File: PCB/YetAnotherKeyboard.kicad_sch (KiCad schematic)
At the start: 15 parts, among them SW88 SW_SPDT, U1 TP4056-42-ESOP8, U2 ER_OLEDM0.91_1x-I2C

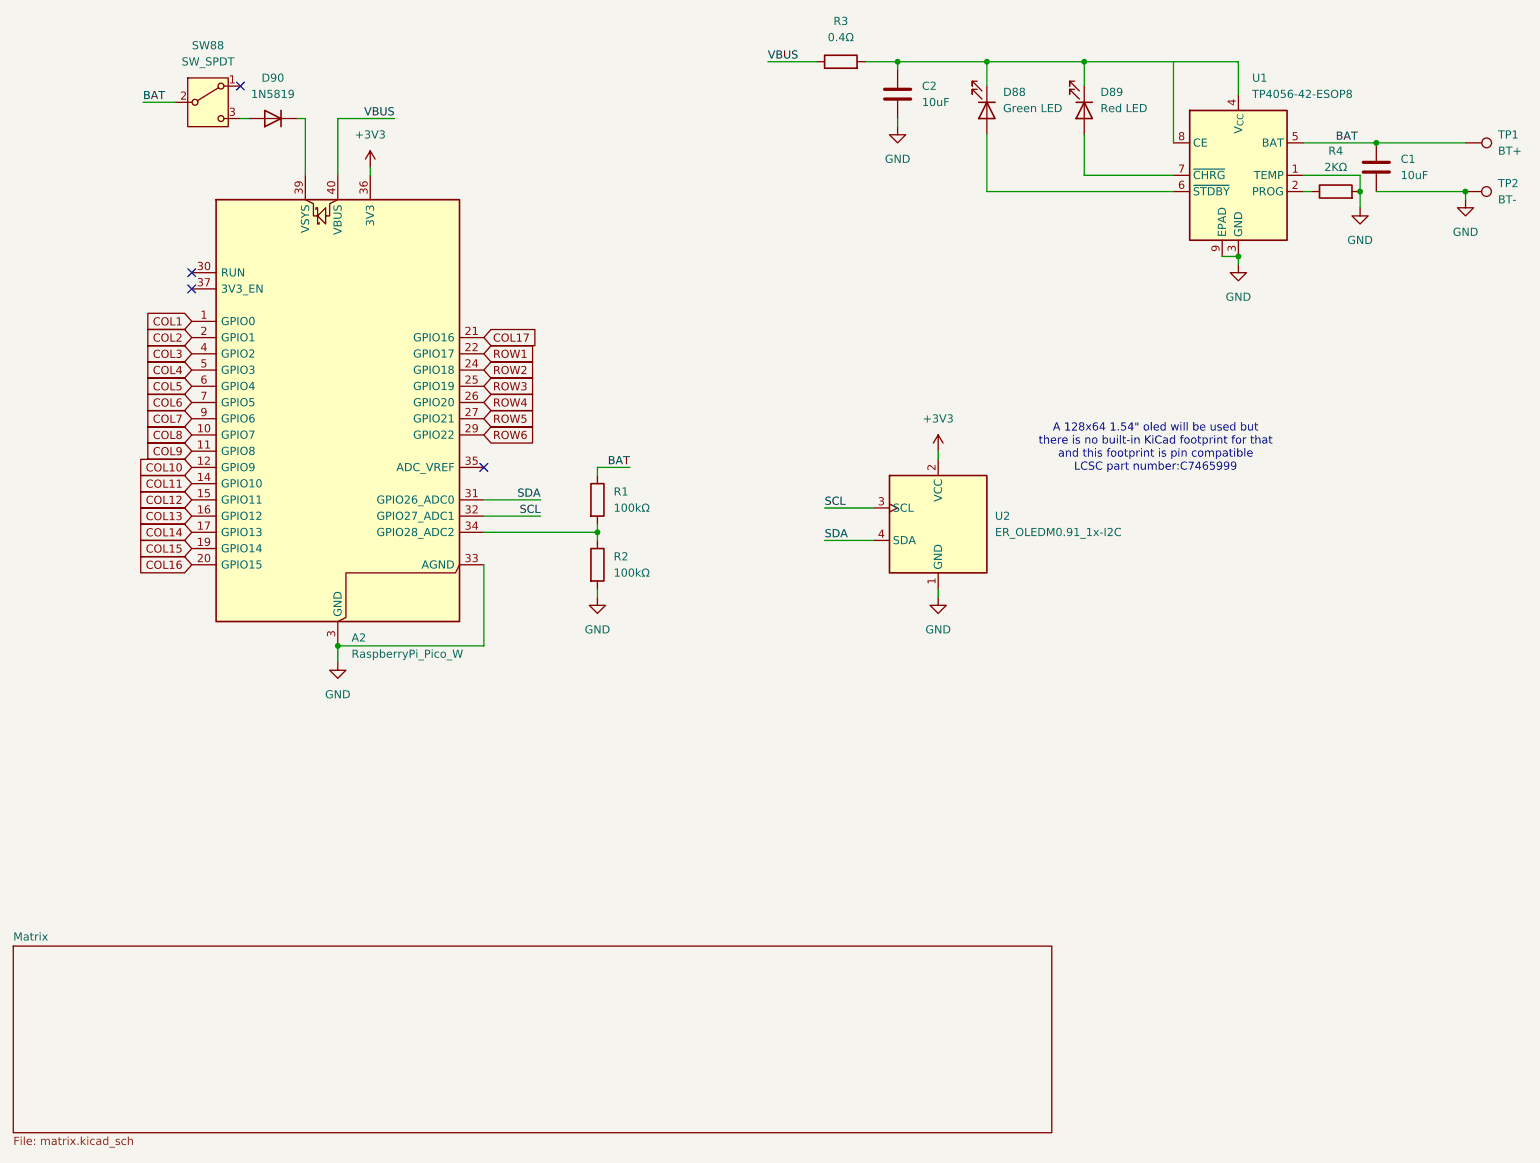
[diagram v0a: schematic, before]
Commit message: change schema to nice! compenents
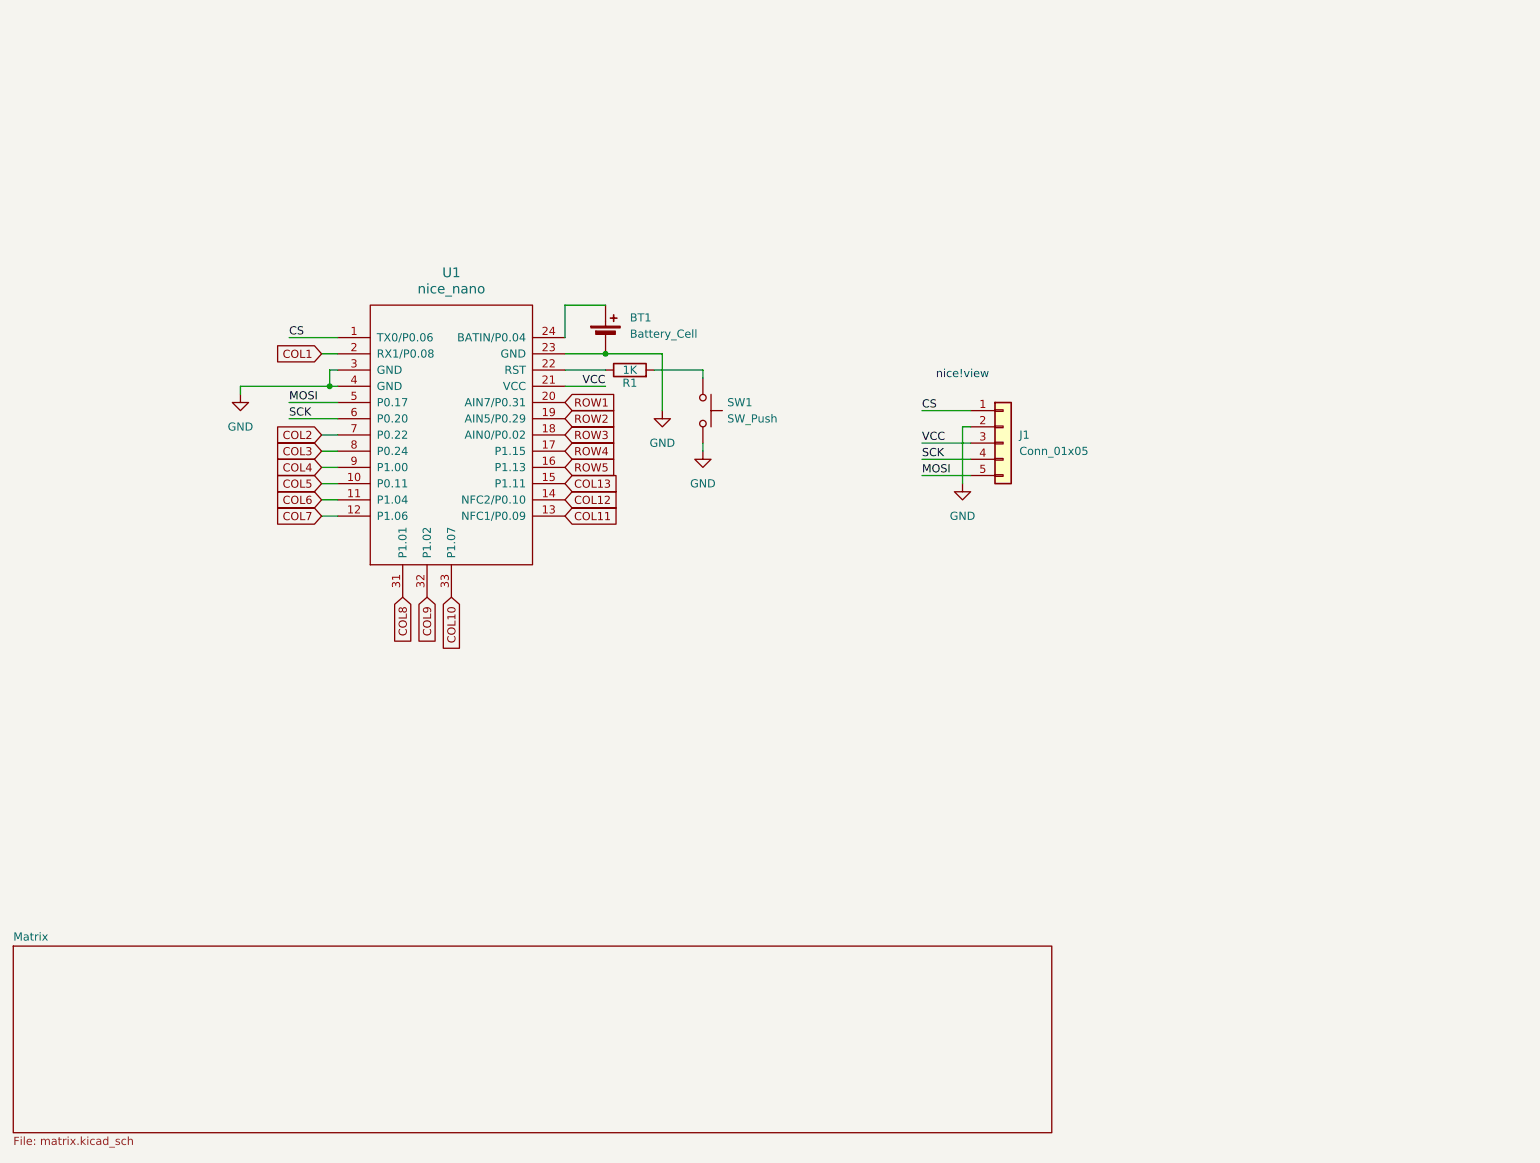
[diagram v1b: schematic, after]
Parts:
- removed A2: RaspberryPi_Pico_W, Module:RaspberryPi_Pico_W_SMD_HandSolder, symbol MCU_Module:RaspberryPi_Pico_W
- removed C1, C2: 10uF, Capacitor_SMD:C_0402_1005Metric, symbol Device:C
- removed D88: Green LED, LED_SMD:LED_0603_1608Metric, symbol Device:LED
- removed D89: Red LED, LED_SMD:LED_0603_1608Metric, symbol Device:LED
- removed D90: 1N5819, Diode_THT:D_DO-41_SOD81_P7.62mm_Horizontal, symbol Device:D
- removed R2: 100kΩ, Resistor_SMD:R_0402_1005Metric, symbol Device:R
- removed R3: 0.4Ω, Resistor_SMD:R_0402_1005Metric, symbol Device:R
- removed R4: 2KΩ, Resistor_SMD:R_0402_1005Metric, symbol Device:R
- removed SW88: SW_SPDT, Button_Switch_SMD:SW_SPDT_Shouhan_MSK12C02, symbol Switch:SW_SPDT
- removed TP1: BT+, TestPoint:TestPoint_Pad_D4.0mm, symbol Connector:TestPoint
- removed TP2: BT-, TestPoint:TestPoint_Pad_D4.0mm, symbol Connector:TestPoint
- removed U1: TP4056-42-ESOP8, Package_SO:SOIC-8-1EP_3.9x4.9mm_P1.27mm_EP2.41x3.3mm_ThermalVias, symbol Battery_Management:TP4056-42-ESOP8
- removed U2: ER_OLEDM0.91_1x-I2C, Display:ER_OLEDM0.91_1x-I2C, symbol Display_Graphic:ER_OLEDM0.91_1x-I2C
- added BT1: Battery_Cell, symbol Device:Battery_Cell
- added J1: Conn_01x05, symbol Connector_Generic:Conn_01x05
- added SW1: SW_Push, symbol Switch:SW_Push
- added U1: nice_nano, symbol nice_nano:nice_nano
- R1: value 100kΩ -> 1K; footprint Resistor_SMD:R_0402_1005Metric -> (none)
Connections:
- net COL1: now also U1.2 (RX1/P0.08)
- net COL10: now also U1.33 (P1.07)
- net COL11: now also U1.13 (NFC1/P0.09)
- net COL12: now also U1.14 (NFC2/P0.10)
- net COL13: now also U1.15 (P1.11)
- net COL2: now also U1.7 (P0.22)
- net COL3: now also U1.8 (P0.24)
- net COL4: now also U1.9 (P1.00)
- net COL5: now also U1.10 (P0.11)
- net COL6: now also U1.11 (P1.04)
- net COL7: now also U1.12 (P1.06)
- net COL8: now also U1.31 (P1.01)
- net COL9: now also U1.32 (P1.02)
- net GND: now also BT1.2 (-), J1.2 (Pin_2), SW1.2, U1.23 (GND), U1.3 (GND), U1.4 (GND)
- net ROW1: now also U1.20 (AIN7/P0.31)
- net ROW2: now also U1.19 (AIN5/P0.29)
- net ROW3: now also U1.18 (AIN0/P0.02)
- net ROW4: now also U1.17 (P1.15)
- net ROW5: now also U1.16 (P1.13)
- net at R1.2: now also SW1.1
- net BAT: no longer names the net of R1.1
- net BAT: now also U1.22 (RST)
- new net: BT1.1 (+), U1.24 (BATIN/P0.04)
- new net CS: J1.1 (Pin_1), U1.1 (TX0/P0.06)
- new net MOSI: J1.5 (Pin_5), U1.5 (P0.17)
- new net SCK: J1.4 (Pin_4), U1.6 (P0.20)
- new net VCC: J1.3 (Pin_3), U1.21 (VCC)
- no-connect marks 4 -> 0
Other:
- note added: "nice!view"
- note removed: "A 128x64 1.54" oled will be used but there is no built-in KiCad footprint for that and this footprint is pin compatible LCSC part number:C7465999"

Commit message: 65% pcb
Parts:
- removed BT1: Battery_Cell, symbol Device:Battery_Cell
- added TP1: BAT, TestPoint:TestPoint_Pad_D2.0mm, symbol Connector:TestPoint
- added TP2: GND, TestPoint:TestPoint_Pad_D2.0mm, symbol Connector:TestPoint
- J1: footprint (none) -> Connector_PinHeader_1.27mm:PinHeader_1x05_P1.27mm_Horizontal
- R1: footprint (none) -> Resistor_SMD:R_0402_1005Metric
- SW1: footprint (none) -> Button_Switch_SMD:SW_Push_SPST_NO_Alps_SKRK
- U1: footprint (none) -> nice_nano:nice_nano
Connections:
- net GND: now also TP2.1
- net at U1.24 (BATIN/P0.04): now also TP1.1
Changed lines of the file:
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@@
 	)
 	(junction
-		(at 106.68 73.66)
+		(at 115.57 73.66)
 		(diameter 0)
 		(color 0 0 0 0)
@@
 	(wire
 		(pts
-			(xy 100.33 71.12) (xy 100.33 66.04)
-		)
-		(stroke
-			(width 0)
-			(type default)
-		)
-	)
-	(wire
-		(pts
 			(xy 63.5 78.74) (xy 49.53 78.74)
 		)
@@
 	(wire
 		(pts
-			(xy 100.33 73.66) (xy 106.68 73.66)
-		)
-		(stroke
-			(width 0)
-			(type default)
-		)
-	)
-	(wire
-		(pts
-			(xy 106.68 73.66) (xy 115.57 73.66)
+			(xy 100.33 73.66) (xy 115.57 73.66)
 		)
 		(stroke
@@
 	(wire
 		(pts
-			(xy 100.33 66.04) (xy 106.68 66.04)
+			(xy 115.57 73.66) (xy 127 73.66)
+		)
+		(stroke
+			(width 0)
+			(type default)
+		)
+	)
+	(wire
+		(pts
+			(xy 100.33 71.12) (xy 106.68 71.12)
 		)
 		(stroke
@@
 		(dnp no)
 		(fields_autoplaced yes)
-		(property "Reference" "#PWR02"
+		(property "Reference" "#PWR04"
 			(at 162.56 100.33 0)
 			(hide yes)
@@
 			(project "YetAnotherKeyboard"
 				(path "/d0add6f3-bc69-47c9-8a57-22475b999a3a"
-					(reference "#PWR02")
+					(reference "#PWR04")
 					(unit 1)
 				)
@@
 		(dnp no)
 		(fields_autoplaced yes)
-		(property "Reference" "#PWR04"
+		(property "Reference" "#PWR01"
 			(at 49.53 86.36 0)
 			(hide yes)
@@
 			(project "YetAnotherKeyboard"
 				(path "/d0add6f3-bc69-47c9-8a57-22475b999a3a"
-					(reference "#PWR04")
+					(reference "#PWR01")
 					(unit 1)
 				)
@@
 		(dnp no)
 		(fields_autoplaced yes)
-		(property "Reference" "#PWR01"
+		(property "Reference" "#PWR03"
 			(at 121.92 95.25 0)
 			(hide yes)
@@
 			(project "YetAnotherKeyboard"
 				(path "/d0add6f3-bc69-47c9-8a57-22475b999a3a"
-					(reference "#PWR01")
+					(reference "#PWR03")
 					(unit 1)
 				)
@@
 			)
 		)
-		(property "Footprint" ""
+		(property "Footprint" "nice_nano:nice_nano"
 			(at 109.22 148.59 90)
 			(hide yes)
@@
 				(path "/d0add6f3-bc69-47c9-8a57-22475b999a3a"
 					(reference "U1")
+					(unit 1)
+				)
+			)
+		)
+	)
+	(symbol
+		(lib_id "Connector:TestPoint")
+		(at 106.68 71.12 270)
+		(unit 1)
+		(body_style 1)
+		(exclude_from_sim no)
+		(in_bom yes)
+		(on_board yes)
+		(in_pos_files yes)
+		(dnp no)
+		(fields_autoplaced yes)
+		(property "Reference" "TP1"
+			(at 111.76 69.8499 90)
+			(show_name no)
+			(do_not_autoplace no)
+			(effects
+				(font
+					(size 1.27 1.27)
+				)
+				(justify left)
+			)
+		)
+		(property "Value" "BAT"
+			(at 111.76 72.3899 90)
+			(show_name no)
+			(do_not_autoplace no)
+			(effects
+				(font
+					(size 1.27 1.27)
+				)
+				(justify left)
+			)
+		)
+		(property "Footprint" "TestPoint:TestPoint_Pad_D2.0mm"
+			(at 106.68 76.2 0)
+			(hide yes)
+			(show_name no)
+			(do_not_autoplace no)
+			(effects
+				(font
+					(size 1.27 1.27)
+				)
+			)
+		)
+		(property "Datasheet" ""
+			(at 106.68 76.2 0)
+			(hide yes)
+			(show_name no)
+			(do_not_autoplace no)
+			(effects
+				(font
+					(size 1.27 1.27)
+				)
+			)
+		)
+		(property "Description" "test point"
+			(at 106.68 71.12 0)
+			(hide yes)
+			(show_name no)
+			(do_not_autoplace no)
+			(effects
+				(font
+					(size 1.27 1.27)
+				)
+			)
+		)
+		(pin "1"
+		)
+		(instances
+			(project "YetAnotherKeyboard"
+				(path "/d0add6f3-bc69-47c9-8a57-22475b999a3a"
+					(reference "TP1")
 					(unit 1)
 				)
@@
 			)
 		)
-		(property "Footprint" ""
+		(property "Footprint" "Connector_PinHeader_1.27mm:PinHeader_1x05_P1.27mm_Horizontal"
 			(at 168.91 87.63 0)
 			(hide yes)
@@
 				(path "/d0add6f3-bc69-47c9-8a57-22475b999a3a"
 					(reference "J1")
-					(unit 1)
-				)
-			)
-		)
-	)
-	(symbol
-		(lib_id "Device:Battery_Cell")
-		(at 106.68 71.12 0)
-		(unit 1)
-		(body_style 1)
-		(exclude_from_sim no)
-		(in_bom yes)
-		(on_board yes)
-		(in_pos_files yes)
-		(dnp no)
-		(fields_autoplaced yes)
-		(property "Reference" "BT1"
-			(at 110.49 68.0084 0)
-			(show_name no)
-			(do_not_autoplace no)
-			(effects
-				(font
-					(size 1.27 1.27)
-				)
-				(justify left)
-			)
-		)
-		(property "Value" "Battery_Cell"
-			(at 110.49 70.5484 0)
-			(show_name no)
-			(do_not_autoplace no)
-			(effects
-				(font
-					(size 1.27 1.27)
-				)
-				(justify left)
-			)
-		)
-		(property "Footprint" ""
-			(at 106.68 69.596 90)
-			(hide yes)
-			(show_name no)
-			(do_not_autoplace no)
-			(effects
-				(font
-					(size 1.27 1.27)
-				)
-			)
-		)
-		(property "Datasheet" ""
-			(at 106.68 69.596 90)
-			(hide yes)
-			(show_name no)
-			(do_not_autoplace no)
-			(effects
-				(font
-					(size 1.27 1.27)
-				)
-			)
-		)
-		(property "Description" "Single-cell battery"
-			(at 106.68 71.12 0)
-			(hide yes)
-			(show_name no)
-			(do_not_autoplace no)
-			(effects
-				(font
-					(size 1.27 1.27)
-				)
-			)
-		)
-		(property "Sim.Device" "V"
-			(at 106.68 71.12 0)
-			(hide yes)
-			(show_name no)
-			(do_not_autoplace no)
-			(effects
-				(font
-					(size 1.27 1.27)
-				)
-			)
-		)
-		(property "Sim.Type" "DC"
-			(at 106.68 71.12 0)
-			(hide yes)
-			(show_name no)
-			(do_not_autoplace no)
-			(effects
-				(font
-					(size 1.27 1.27)
-				)
-			)
-		)
-		(property "Sim.Pins" "1=+ 2=-"
-			(at 106.68 71.12 0)
-			(hide yes)
-			(show_name no)
-			(do_not_autoplace no)
-			(effects
-				(font
-					(size 1.27 1.27)
-				)
-			)
-		)
-		(pin "1"
-		)
-		(pin "2"
-		)
-		(instances
-			(project "YetAnotherKeyboard"
-				(path "/d0add6f3-bc69-47c9-8a57-22475b999a3a"
-					(reference "BT1")
 					(unit 1)
 				)
@@
 			)
 		)
-		(property "Footprint" ""
+		(property "Footprint" "Resistor_SMD:R_0402_1005Metric"
 			(at 110.49 77.978 90)
 			(hide yes)
@@
 			)
 		)
-		(property "Footprint" ""
+		(property "Footprint" "Button_Switch_SMD:SW_Push_SPST_NO_Alps_SKRK"
 			(at 127 82.55 0)
 			(hide yes)
@@
 		(dnp no)
 		(fields_autoplaced yes)
-		(property "Reference" "#PWR03"
+		(property "Reference" "#PWR02"
 			(at 115.57 88.9 0)
 			(hide yes)
@@
 			(project "YetAnotherKeyboard"
 				(path "/d0add6f3-bc69-47c9-8a57-22475b999a3a"
-					(reference "#PWR03")
+					(reference "#PWR02")
 					(unit 1)
 				)
+			)
+		)
+	)
+	(symbol
+		(lib_id "Connector:TestPoint")
+		(at 127 73.66 270)
+		(unit 1)
+		(body_style 1)
+		(exclude_from_sim no)
+		(in_bom yes)
+		(on_board yes)
+		(in_pos_files yes)
+		(dnp no)
+		(fields_autoplaced yes)
+		(property "Reference" "TP2"
+			(at 132.08 72.3899 90)
+			(show_name no)
+			(do_not_autoplace no)
+			(effects
+				(font
+					(size 1.27 1.27)
+				)
+				(justify left)
+			)
+		)
+		(property "Value" "GND"
+			(at 132.08 74.9299 90)
+			(show_name no)
+			(do_not_autoplace no)
+			(effects
+				(font
+					(size 1.27 1.27)
+				)
+				(justify left)
+			)
+		)
+		(property "Footprint" "TestPoint:TestPoint_Pad_D2.0mm"
+			(at 127 78.74 0)
+			(hide yes)
+			(show_name no)
+			(do_not_autoplace no)
+			(effects
+				(font
+					(size 1.27 1.27)
+				)
+			)
+		)
+		(property "Datasheet" ""
+			(at 127 78.74 0)
+			(hide yes)
+			(show_name no)
+			(do_not_autoplace no)
+			(effects
+				(font
+					(size 1.27 1.27)
+				)
+			)
+		)
+		(property "Description" "test point"
+			(at 127 73.66 0)
+			(hide yes)
+			(show_name no)
+			(do_not_autoplace no)
+			(effects
+				(font
+					(size 1.27 1.27)
+				)
+			)
+		)
+		(pin "1"
+		)
+		(instances
+			(project "YetAnotherKeyboard"
+				(path "/d0add6f3-bc69-47c9-8a57-22475b999a3a"
+					(reference "TP2")
+					(unit 1)
+				)

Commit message: 3d models
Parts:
- J1: footprint Connector_PinHeader_1.27mm:PinHeader_1x05_P1.27mm_Horizontal -> Connector_PinHeader_2.54mm:PinHeader_1x05_P2.54mm_Vertical
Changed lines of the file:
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@@
 			)
 		)
-		(property "Footprint" "Connector_PinHeader_1.27mm:PinHeader_1x05_P1.27mm_Horizontal"
+		(property "Footprint" "Connector_PinHeader_2.54mm:PinHeader_1x05_P2.54mm_Vertical"
 			(at 168.91 87.63 0)
 			(hide yes)
